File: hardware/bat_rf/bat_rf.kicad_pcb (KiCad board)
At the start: 2 copper layers, 13.2 x 6 mm, 83 parts, among them J1 USB_C_Receptacle_PowerOnly_6P, J3 burningPort, J4 Conn_01x02, J5 Conn_01x04, Q1 NMOS, SW2 RESET, SW3 SW_DPDT_x2, U1 TPS54331, U3 ESP8684-WROOM-02UC, U4 CS5090E

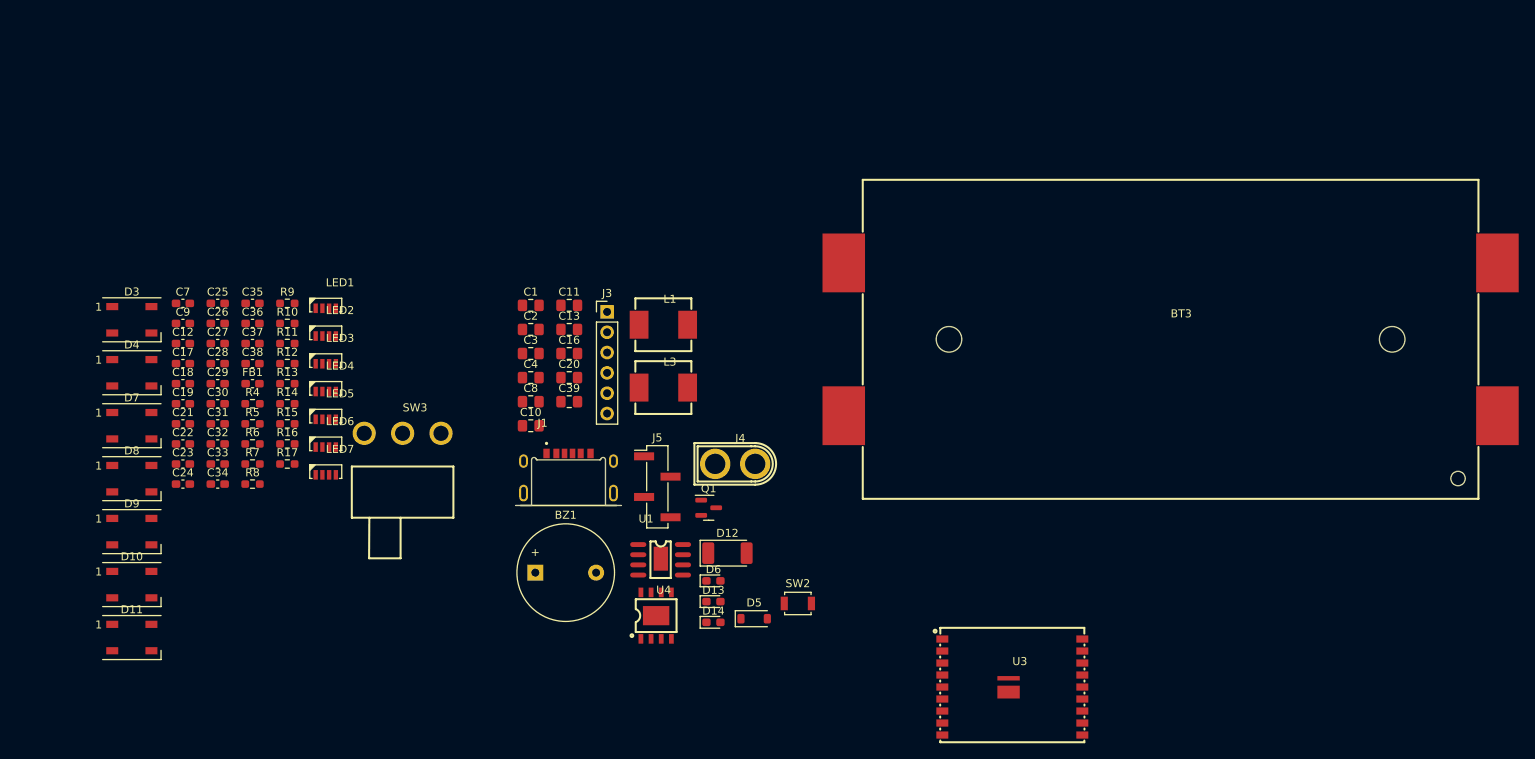
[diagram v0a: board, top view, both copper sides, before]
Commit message: esp32 sch update
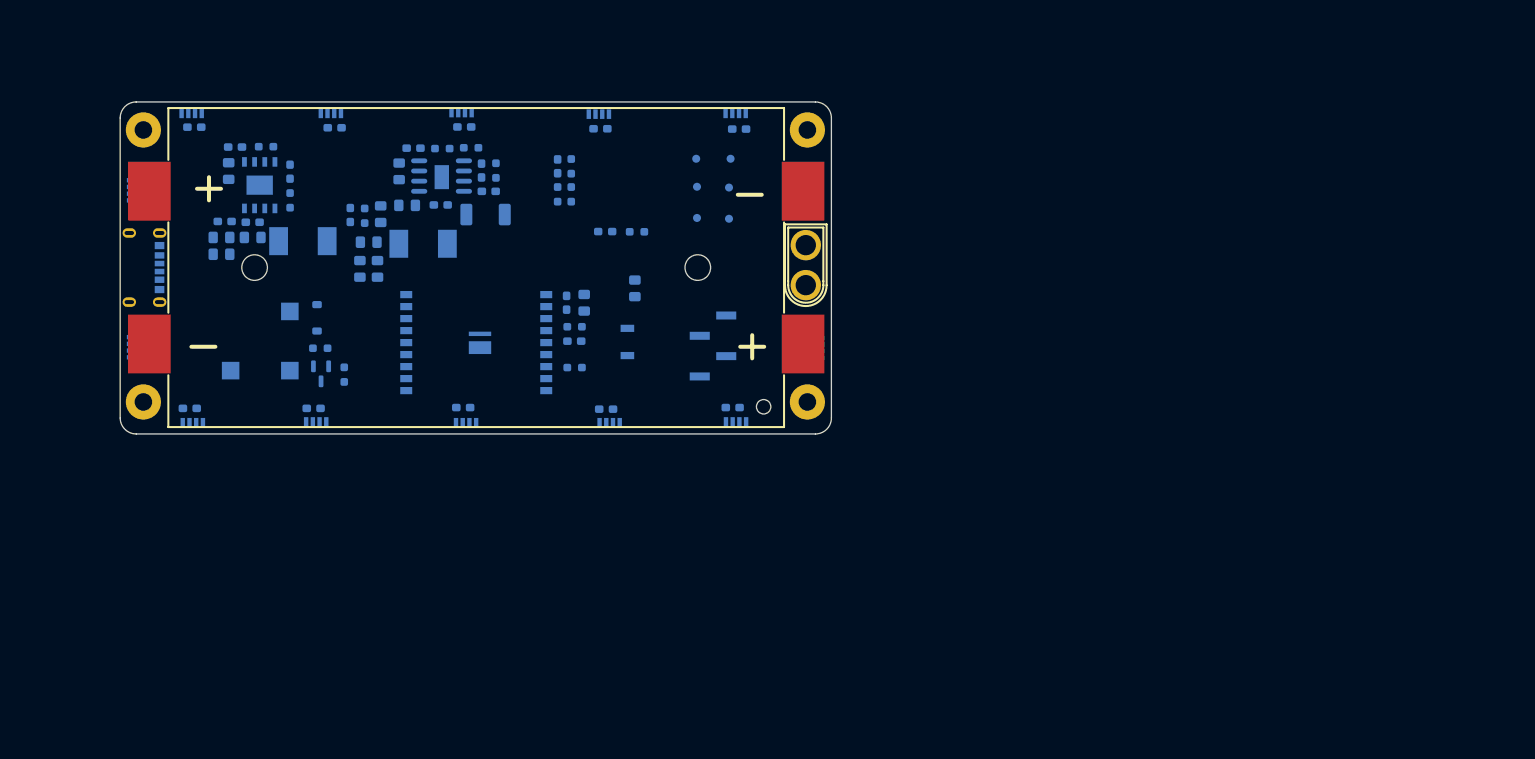
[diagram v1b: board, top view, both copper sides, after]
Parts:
- removed BT3: Battery, bat_rf:BAT-SMD_BH-18650-B1BA007
- removed C26, C27, C28, C29: 100n, Capacitor_SMD:C_0603_1608Metric_Pad1.08x0.95mm_HandSolder
- removed D10, D11, D3, D4, D7, D8, D9: WS2812B, LED_SMD:LED_WS2812B_PLCC4_5.0x5.0mm_P3.2mm
- removed J3: burningPort, Connector_PinHeader_2.54mm:PinHeader_1x06_P2.54mm_Vertical
- removed SW3: SW_DPDT_x2, bat_rf:SW-TH_3P-SS12D06-1
- added BT1: doubleBatCell, bat_rf:BAT-SMD_BH-18650-B1BA007, F.Cu at (88.1, 71.7)
- added C14: 100n, Capacitor_SMD:C_0603_1608Metric_Pad1.08x0.95mm_HandSolder, B.Cu at (120.9, 54.4)
- added C15: 100n, Capacitor_SMD:C_0603_1608Metric_Pad1.08x0.95mm_HandSolder, B.Cu at (70.4, 54.2)
- added C5: 100n, Capacitor_SMD:C_0603_1608Metric_Pad1.08x0.95mm_HandSolder, B.Cu at (86.6, 54.1)
- added C6: 100n, Capacitor_SMD:C_0603_1608Metric_Pad1.08x0.95mm_HandSolder, B.Cu at (103.6, 54.3)
- added H1: MountingHole, MountingHole:MountingHole_2.2mm_M2_Pad, F.Cu at (46.5, 54.5)
- added H2: MountingHole, MountingHole:MountingHole_2.2mm_M2_Pad, F.Cu at (129.5, 54.5)
- added H3: MountingHole, MountingHole:MountingHole_2.2mm_M2_Pad, F.Cu at (129.5, 88.5)
- added H4: MountingHole, MountingHole:MountingHole_2.2mm_M2_Pad, F.Cu at (46.5, 88.5)
- added LED10: XL-4020RGBC-WS2812B, bat_rf:LED-SMD_4P-L4.0-W1.7_M4020-03003-RGB-862-001, B.Cu at (120.5, 52.4)
- added LED11: XL-4020RGBC-WS2812B, bat_rf:LED-SMD_4P-L4.0-W1.7_M4020-03003-RGB-862-001, B.Cu at (69.9, 52.4)
- added LED12: XL-4020RGBC-WS2812B, bat_rf:LED-SMD_4P-L4.0-W1.7_M4020-03003-RGB-862-001, B.Cu at (52.5, 52.4)
- added LED13: XL-4020RGBC-WS2812B, bat_rf:LED-SMD_4P-L4.0-W1.7_M4020-03003-RGB-862-001, B.Cu at (45.0, 62.0)
- added LED14: XL-4020RGBC-WS2812B, bat_rf:LED-SMD_4P-L4.0-W1.7_M4020-03003-RGB-862-001, B.Cu at (45.0, 81.6)
- added LED8: XL-4020RGBC-WS2812B, bat_rf:LED-SMD_4P-L4.0-W1.7_M4020-03003-RGB-862-001, B.Cu at (86.2, 52.3)
- added LED9: XL-4020RGBC-WS2812B, bat_rf:LED-SMD_4P-L4.0-W1.7_M4020-03003-RGB-862-001, B.Cu at (103.4, 52.5)
- added TP1: TestPoint, TestPoint:TestPoint_Pad_D1.0mm, B.Cu at (119.9, 58.1)
- added TP2: TestPoint, TestPoint:TestPoint_Pad_D1.0mm, B.Cu at (115.7, 61.6)
- added TP3: TestPoint, TestPoint:TestPoint_Pad_D1.0mm, B.Cu at (115.6, 58.1)
- added TP4: TestPoint, TestPoint:TestPoint_Pad_D1.0mm, B.Cu at (119.7, 65.6)
- added TP5: TestPoint, TestPoint:TestPoint_Pad_D1.0mm, B.Cu at (119.7, 61.7)
- added TP6: TestPoint, TestPoint:TestPoint_Pad_D1.0mm, B.Cu at (115.7, 65.5)
- BZ1: footprint Buzzer_Beeper:Buzzer_12x9.5RM7.6 -> Buzzer_Beeper:MagneticBuzzer_Kobitone_254-EMB84Q-RO; moved to B.Cu
- C1, C10, C11, C12, C13, C16, C17, C18, C19, C2, C20, C21, C22, C23, C24, C25, C3, C30, C31, C32, C33, C34, C35, C36, C37, C38, C39, C4, C7, C8, C9, D12, D13, D14, D5, D6, J5, L1, L3, LED1, LED2, LED3, LED4, LED5, LED6, LED7, Q1, R10, R11, R12, R13, R14, R15, R16, R17, R4, R5, R6, R7, R8, R9, SW2, U1, U3, U4: moved to B.Cu
- FB1: footprint Capacitor_SMD:C_0603_1608Metric_Pad1.08x0.95mm_HandSolder -> Capacitor_SMD:C_0805_2012Metric_Pad1.18x1.45mm_HandSolder; moved to B.Cu
- J1: footprint bat_rf:GCT_USB4515-GF-A_REVA -> bat_rf:USB-C-SMD_HX-TYPE-C-6PIN; moved to B.Cu
- moved U3 79.7 mm to (88.1, 81.1), turned to 180 degrees
- moved C30 77.9 mm to (128.9, 61.9), turned to 90 degrees
- moved C31 73.8 mm to (129.0, 82.0), turned to 90 degrees
- moved D6 73.6 mm to (64.8, 59.7), turned to -90 degrees
- moved U4 73.2 mm to (61.0, 61.4), turned to 180 degrees
- moved D14 68.2 mm to (72.3, 65.1), turned to 90 degrees
- moved D5 66.3 mm to (68.2, 78.0), turned to -90 degrees
- moved C32 64.5 mm to (120.1, 89.2)
- moved LED1 63.5 mm to (130.9, 61.5), turned to 90 degrees
- moved LED2 61.8 mm to (131.0, 81.7), turned to 90 degrees
- moved J1 60.0 mm to (46.6, 71.7), turned to 90 degrees
- moved D12 52.0 mm to (89.2, 65.0)
- moved U1 51.9 mm to (81.0, 62.2)
- moved LED3 51.8 mm to (120.5, 91.0)
- moved Q1 51.3 mm to (68.7, 85.0), turned to -90 degrees
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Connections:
- C36 pad 2: Net-(LED7-VDD) -> +3V3
- D13 pad 1: GNDPWR -> /LED
- J4 pad 1: Net-(J4-Pin_1) -> +BATT
- LED7 pad 3: Net-(LED7-VDD) -> +3V3
- U3 pad 10: unconnected-(U3-IO10-Pad10) -> /RGB
- U3 pad 14: unconnected-(U3-IO18-Pad14) -> /beep
- U3 pad 15: /RGB -> unconnected-(U3-IO3-Pad15)
- U3 pad 16: /beep -> unconnected-(U3-IO2-Pad16)
- U3 pad 17: /ESP_RX -> /LED
- U3 pad 18: /ESP_TX -> /BAT_FB
- U3 pad 4: GNDPWR -> unconnected-(U3-IO5-Pad4)
- U3 pad 5: /BAT_FB -> /ESP_TX
- U3 pad 6: unconnected-(U3-IO7-Pad6) -> /ESP_RX
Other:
- board size 13.2 x 6 mm -> 88.9 x 41.5 mm
- board text added: "+3V3"
- board text added: "0.0000 mm / 0.0000 mm"
- board text added: "0.3000 mm"
- board text added: "1.6000 mm"
- board text added: "2"
- board text added: "3V3"
- board text added: "88.9000 mm x 41.5000 mm"
- board text added: "BAT_V"
- board text added: "BOARD CHARACTERISTICS"
- board text added: "BOOT"
- board text added: "CHARGER"
- board text added: "DC-DC(3.3V)"
- board text added: "EN"
- board text added: "GND"
- board text added: "LED"
- board text added: "MCU"
- board text added: "None"
- board text added: "RESET"
- board text added: "RX"
- board text added: "RXD"
- board text added: "TX"
- board text added: "TXD"
- board text added: "V1.0"
- board text added: "beeper"
- board text added: "否"
- board text added: "孔最小直径："
- board text added: "最小布线/间距："
- board text added: "板子整体尺寸："
- board text added: "电路板厚度："
- board text added: "电镀板边："
- board text added: "边缘卡连接器："
- board text added: "邮票孔："
- board text added: "铜层数量："
- board text added: "铜表面处理（镀铜）："
- board text added: "阻抗控制"

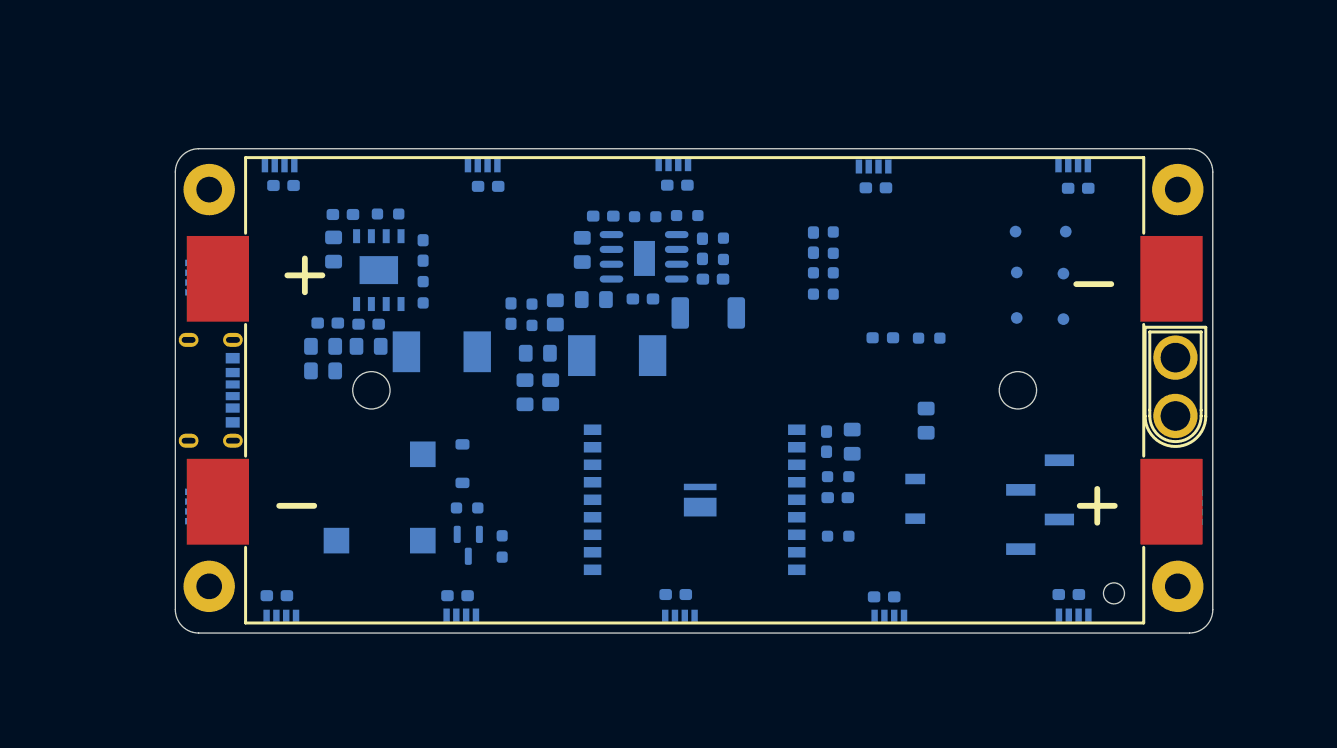
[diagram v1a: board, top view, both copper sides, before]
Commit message: rfBat PCB sent to manufacturing
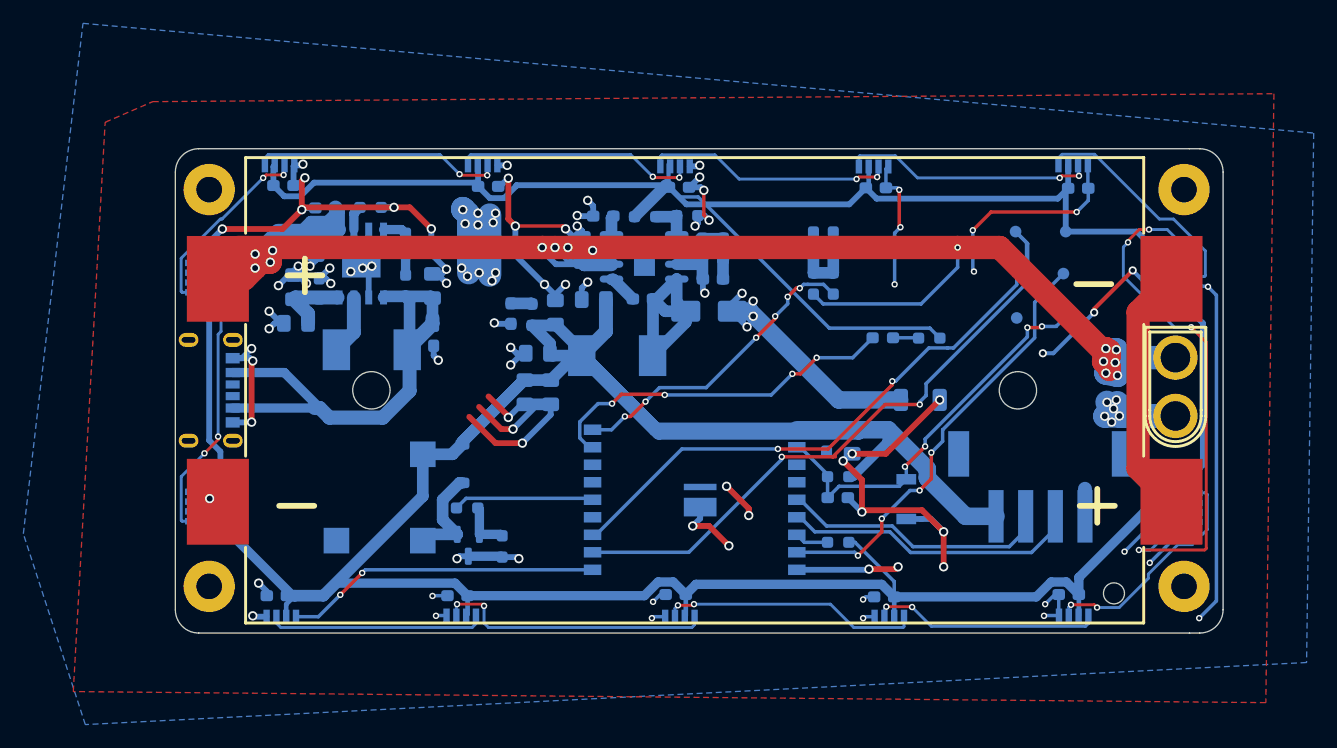
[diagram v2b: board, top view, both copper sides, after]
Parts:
- removed J5: Conn_01x04, Connector_PinHeader_2.54mm:PinHeader_1x04_P2.54mm_Vertical_SMD_Pin1Left
- added J2: Conn_01x04, bat_rf:CONN-SMD_4P-P2.54_XH2.54-4AB_vertical, B.Cu at (117.7, 79.8)
- D12: footprint Diode_SMD:D_MELF -> Diode_SMD:D_SMA
- FB1: footprint Capacitor_SMD:C_0805_2012Metric_Pad1.18x1.45mm_HandSolder -> Inductor_SMD:L_1206_3216Metric_Pad1.22x1.90mm_HandSolder
- moved C8 7.53 mm to (65.6, 62.7), turned to 90 degrees
- moved L1 6.00 mm to (60.4, 68.2), turned to 180 degrees
- moved C11 5.67 mm to (53.7, 62.8), turned to 90 degrees
- moved C7 5.66 mm to (65.7, 67.0), turned to -90 degrees
- moved C10 4.69 mm to (53.9, 65.9), turned to 180 degrees
- moved C9 3.06 mm to (55.9, 62.9), turned to 90 degrees
- moved FB1 1.84 mm to (107.4, 72.5), turned to 0 degrees
- moved C12 1.60 mm to (56.4, 56.0)
- moved C13 1.60 mm to (55.6, 59.0)
- moved D6 1.60 mm to (63.3, 59.1)
- moved R11 1.60 mm to (60.3, 56.0)
- moved R12 1.60 mm to (63.3, 62.7)
- moved U4 1.60 mm to (59.5, 60.8)
- moved SW2 0.77 mm to (106.2, 81.0)
- moved H2 0.53 mm to (130.0, 54.5)
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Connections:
- LED11 pad 2: unconnected-(LED11-DO-Pad2) -> Net-(LED11-DO)
- LED12 pad 2: Net-(LED11-DI) -> Net-(LED12-DO)
- LED12 pad 4: Net-(LED12-DI) -> Net-(LED11-DO)
- LED13 pad 2: Net-(LED12-DI) -> Net-(LED13-DO)
- LED13 pad 4: Net-(LED13-DI) -> Net-(LED12-DO)
- LED14 pad 2: Net-(LED13-DI) -> unconnected-(LED14-DO-Pad2)
- LED14 pad 4: unconnected-(LED14-DI-Pad4) -> Net-(LED13-DO)
- LED8 pad 2: unconnected-(LED8-DO-Pad2) -> Net-(LED11-DI)
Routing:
- net +3V3: track 0.00 -> 433.4 mm
- net GNDPWR: track 0.00 -> 304.9 mm, vias 0 -> 92
- net +BATT: track 0.00 -> 157.1 mm, vias 0 -> 15
- net /RXD: track 0.00 -> 60.0 mm, vias 0 -> 2
- net Net-(U4-VIN): track 0.00 -> 58.9 mm
- net GNDD: track 0.00 -> 51.9 mm, vias 0 -> 12
- net Net-(LED1-DI): track 0.00 -> 49.9 mm, vias 0 -> 4
- net /TXD: track 0.00 -> 46.5 mm, vias 0 -> 2
- net /IO9: track 0.00 -> 37.3 mm, vias 0 -> 4
- net /EN: track 0.00 -> 33.8 mm, vias 0 -> 4
- net /LED: track 0.00 -> 30.9 mm, vias 0 -> 4
- net /RGB: track 0.00 -> 27.1 mm, vias 0 -> 2
- net /ESP_RX: track 0.00 -> 26.9 mm
- net /BAT_FB: track 0.00 -> 26.6 mm, vias 0 -> 6
- net Net-(LED13-DO): track 0.00 -> 25.7 mm, vias 0 -> 2
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- added copper zone on B.Cu, net GNDD
- added copper zone on F.Cu, net GNDPWR
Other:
- board size 88.9 x 41.5 mm -> 89.8 x 41.5 mm
- board text added: "BEEPER"
- board text removed: "beeper"

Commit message: batRf to v1.1
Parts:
- added D1: 3A, Diode_SMD:D_SMA, B.Cu at (55.4, 69.1)
- added TP7: TestPoint, TestPoint:TestPoint_Pad_D1.0mm, B.Cu at (74.8, 80.8)
- added TP8: TestPoint, TestPoint:TestPoint_Pad_D1.0mm, B.Cu at (95.8, 64.5)
- added TP9: TestPoint, TestPoint:TestPoint_Pad_D1.0mm, B.Cu at (76.2, 86.8)
- R16: value 10.2k -> 3.24k
- moved C7 4.30 mm to (69.4, 69.2)
- moved L1 3.04 mm to (63.4, 68.2)
- moved J2 0.20 mm to (117.7, 80.0)
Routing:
- net GNDPWR: track 304.9 -> 292.3 mm
- net Net-(U4-VIN): track 58.9 -> 64.0 mm
- net Net-(D1-K): track 6.40 -> 10.2 mm
- net Net-(D1-A): track 5.10 -> 8.49 mm
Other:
- board text added: "+BAT"
- board text added: "M2"
- board text added: "RGB"
- board text added: "V1.1"
- board text removed: "V1.0"

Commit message: 更新rfBat PCB
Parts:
- removed BT1: doubleBatCell, bat_rf:BAT-SMD_BH-18650-B1BA007
- removed C11: 22u, Capacitor_SMD:C_0805_2012Metric_Pad1.18x1.45mm_HandSolder
- removed C12, C7, C9: 1u, Capacitor_SMD:C_0603_1608Metric_Pad1.08x0.95mm_HandSolder
- removed C13, C8: 10u, Capacitor_SMD:C_0805_2012Metric_Pad1.18x1.45mm_HandSolder
- removed D1: 3A, Diode_SMD:D_SMA
- removed D6: RED, LED_SMD:LED_0603_1608Metric_Pad1.05x0.95mm_HandSolder
- removed L1: 2.2u, bat_rf:IND-SMD_L7.0-W6.6_0630CDMCCDS
- removed R11, R12: 1k, Resistor_SMD:R_0603_1608Metric_Pad0.98x0.95mm_HandSolder
- removed U4: CS5090E, bat_rf:ESOP-8_L4.9-W3.9-P1.27-LS6.0-BL-EP
- added BT2: doubleBatCell, bat_rf:BAT-SMD_BH-18650-B1BA007, F.Cu at (87.9, 71.8)
- added C26: 22u, Capacitor_SMD:C_0805_2012Metric_Pad1.18x1.45mm_HandSolder, B.Cu at (55.9, 60.1)
- added C27: 100n, Capacitor_SMD:C_0603_1608Metric_Pad1.08x0.95mm_HandSolder, B.Cu at (60.4, 69.1)
- added C28: 10u, Capacitor_SMD:C_0805_2012Metric_Pad1.18x1.45mm_HandSolder, B.Cu at (53.1, 68.6)
- added C29: 10u, Capacitor_SMD:C_0805_2012Metric_Pad1.18x1.45mm_HandSolder, B.Cu at (64.3, 69.0)
- added C40: 10u, Capacitor_SMD:C_0805_2012Metric_Pad1.18x1.45mm_HandSolder, B.Cu at (63.1, 56.4)
- added D2: RED, Capacitor_SMD:C_0805_2012Metric_Pad1.18x1.45mm_HandSolder, B.Cu at (66.8, 69.2)
- added L2: 2.2uH, Inductor_SMD_Wurth:L_Wurth_WE-LQSH-4020, B.Cu at (57.0, 68.5)
- added R1: 0.5R, Resistor_SMD:R_0603_1608Metric_Pad0.98x0.95mm_HandSolder, B.Cu at (62.3, 69.2)
- added R18: 51k, Resistor_SMD:R_0603_1608Metric_Pad0.98x0.95mm_HandSolder, B.Cu at (66.7, 60.1)
- added R2: 5k1, Resistor_SMD:R_0603_1608Metric_Pad0.98x0.95mm_HandSolder, B.Cu at (57.2, 64.4)
- added R3: 100R, Resistor_SMD:R_0603_1608Metric_Pad0.98x0.95mm_HandSolder, B.Cu at (66.7, 64.9)
- added U2: IP2325_5M_WHJC, bat_rf:ESOP-8_L4.9-W3.9-P1.27-LS6.0-BL-EP3.1, B.Cu at (62.6, 61.7)
- moved C10 7.30 mm to (58.3, 60.1), turned to -90 degrees
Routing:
- net GNDPWR: track 292.3 -> 250.7 mm, vias 92 -> 76
- net Net-(BT2-+-Pad3): track 0.00 -> 21.5 mm
- net Net-(BT1-+-Pad3): track 21.5 -> 0.00 mm
- net Net-(C28-Pad1): track 64.0 -> 53.3 mm
- net Net-(U2-VIN): track 0.00 -> 10.3 mm
- net Net-(U2-LX): track 0.00 -> 9.25 mm
- net Net-(D1-A): track 8.49 -> 0.00 mm
- net Net-(U2-VSYS): track 10.2 -> 4.77 mm
- net Net-(U2-BST): track 0.00 -> 4.49 mm
- net Net-(D2-A): track 0.00 -> 2.45 mm
- net Net-(U2-LED): track 0.00 -> 2.37 mm
- net Net-(U2-NTC): track 0.00 -> 2.29 mm
- net Net-(U4-ICHG): track 2.11 -> 0.00 mm
- net Net-(D6-K): track 2.03 -> 0.00 mm
- net Net-(D6-A): track 1.80 -> 0.00 mm
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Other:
- board text added: "V1.2"
- board text removed: "V1.1"
